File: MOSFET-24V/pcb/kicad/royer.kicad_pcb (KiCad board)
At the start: 2 copper layers, 53.3 x 73.7 mm, 25 parts, among them J1 9-24V, J2 COIL, Q1 IRFB4410, Q2 IRFD110, Q3 IRFD110, Q4 IRFB4410

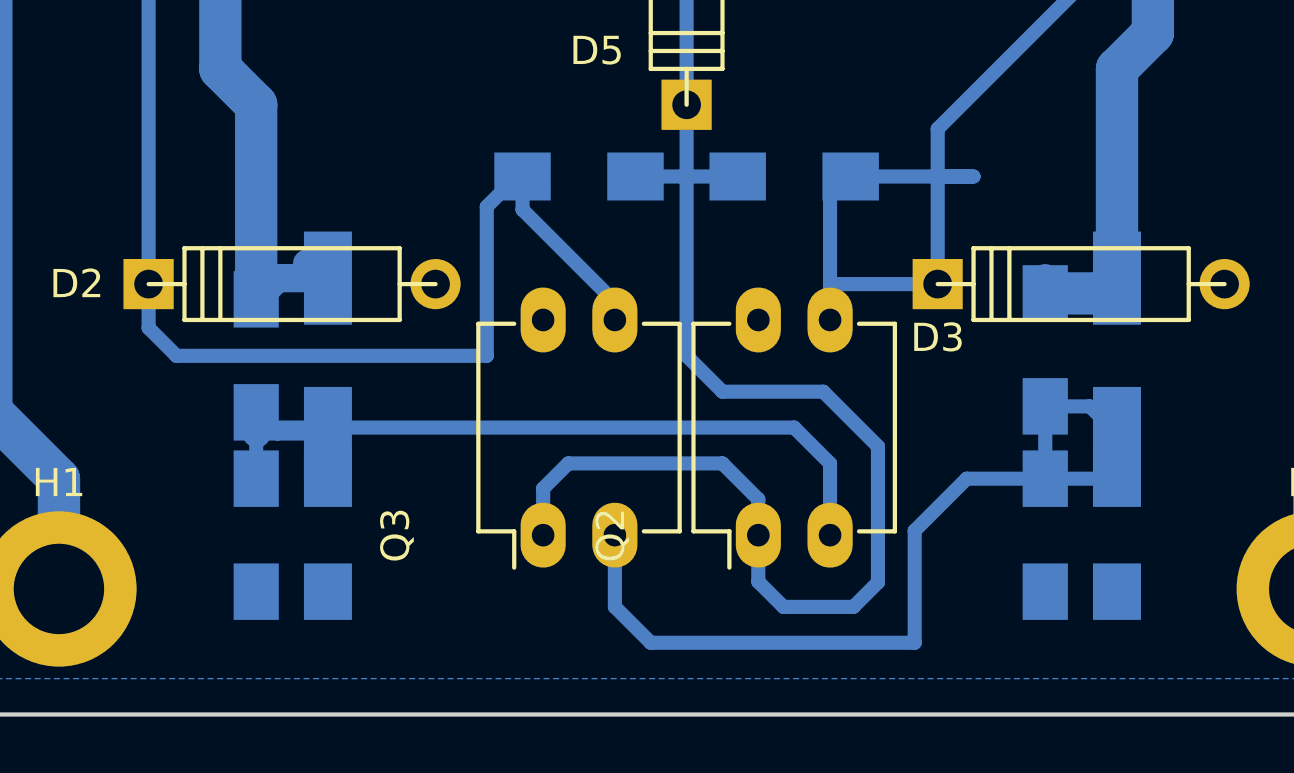
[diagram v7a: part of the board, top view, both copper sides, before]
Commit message: stack DIL-4 end-to-end to fit into a single DIL-8 socket
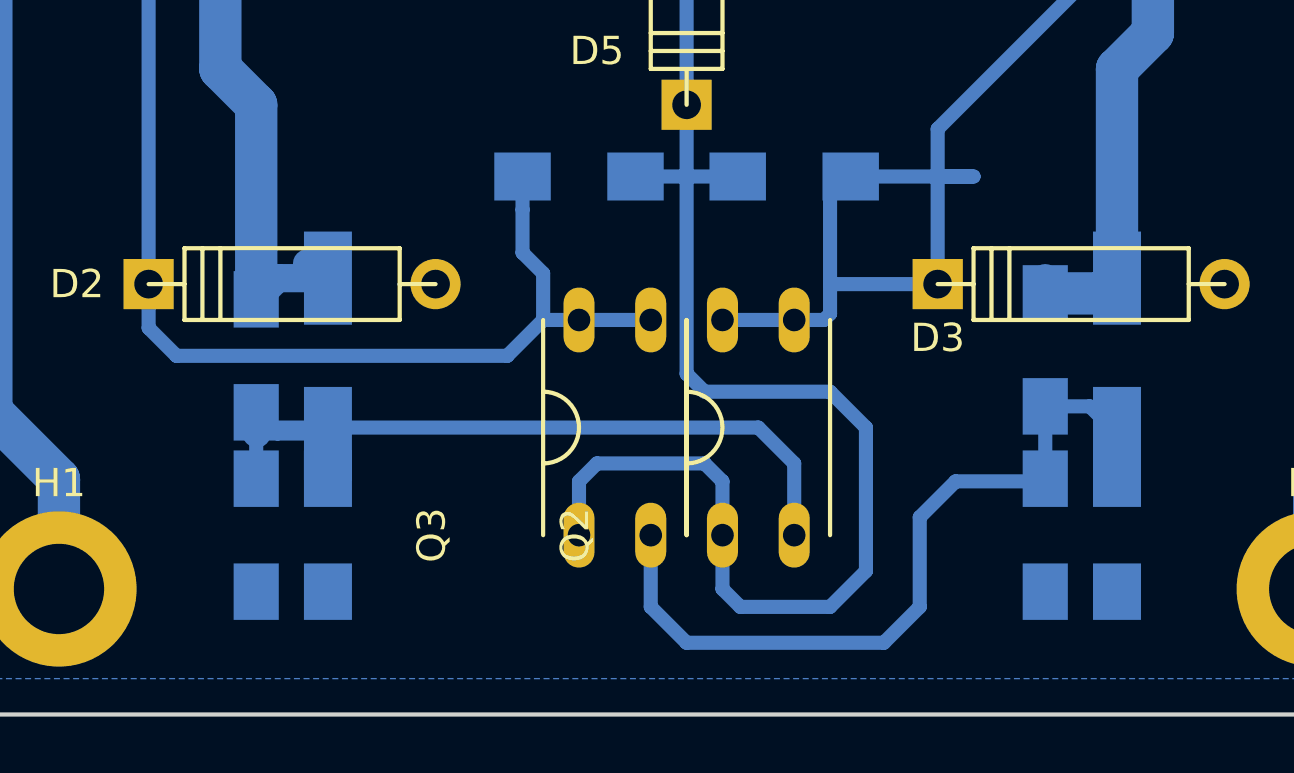
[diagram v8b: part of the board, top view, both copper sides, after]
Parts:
- Q2, Q3: footprint Housings_DIP:DIP-4_W7.62mm_LongPads -> DIL-4:DIP-4_W7.62mm_LongPads
- moved Q2 1.27 mm to (179.1, 137.2)
- moved Q3 1.27 mm to (174.0, 137.2)
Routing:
- net /D2: track 34.2 -> 29.9 mm
- net /G2: track 30.6 -> 34.3 mm
- net /G1: track 42.9 -> 41.3 mm
- net /D1: track 29.5 -> 28.2 mm
- net /9V: track 58.3 -> 57.3 mm
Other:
- net class Default: clearance 0.5 -> 0.4
- rule trace_clearance: 0.5 -> 0.4
